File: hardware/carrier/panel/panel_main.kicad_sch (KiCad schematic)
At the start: 27 parts, among them J1 GDEY029T94 FPC, J2 CARRIER, J3 FL-A FPC (FL03), J4 FL-B FPC (Orient), J5 FRONTLIGHT, Q5 SI1308EDL

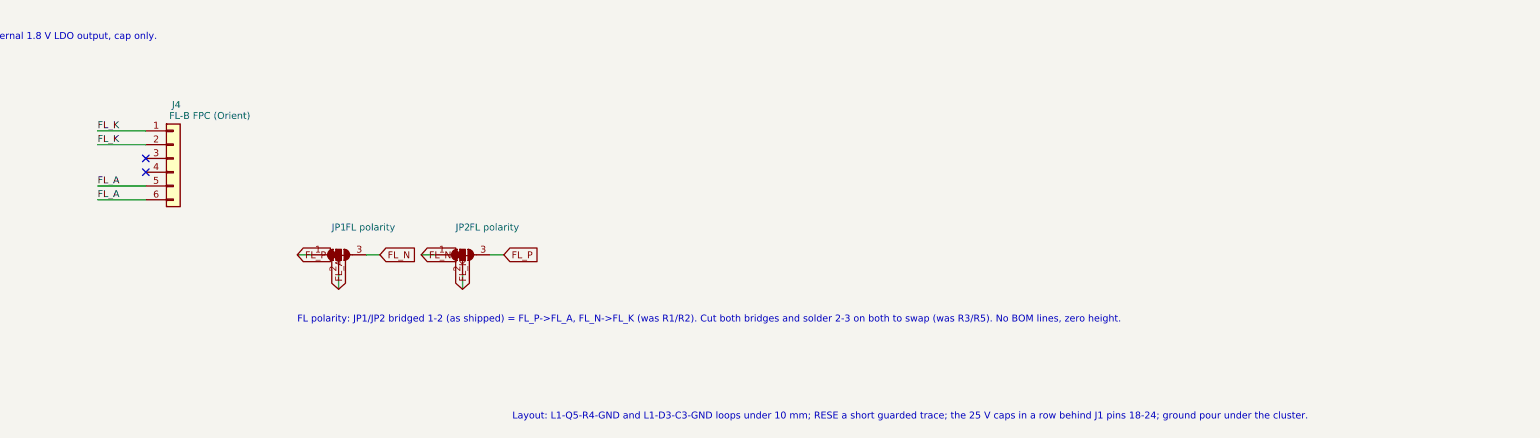
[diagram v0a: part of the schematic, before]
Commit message: Completed the panel board
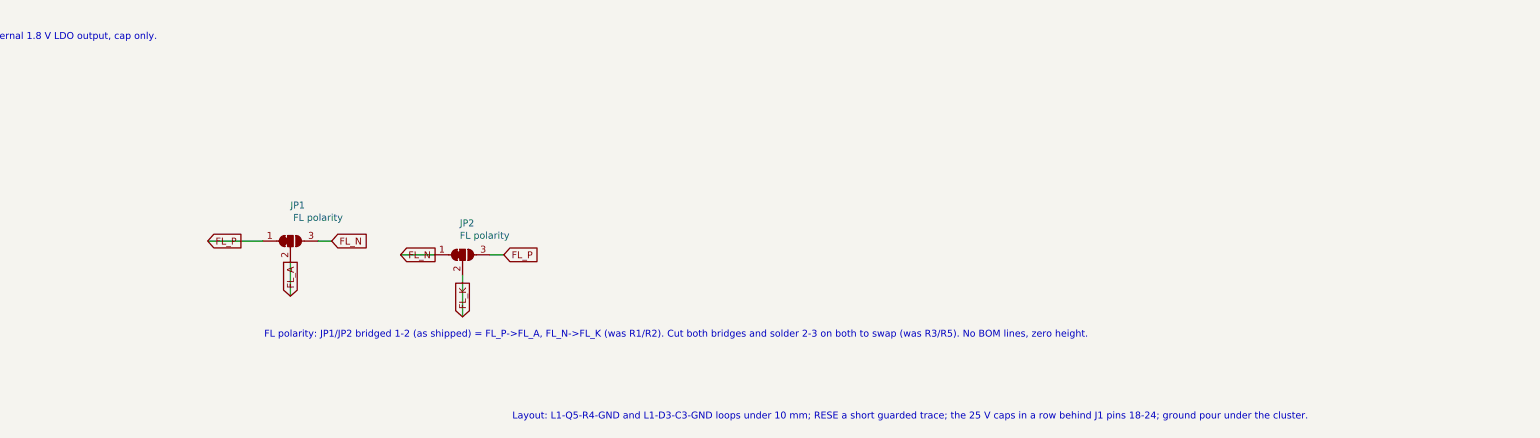
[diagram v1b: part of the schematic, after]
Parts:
- removed J4: FL-B FPC (Orient), pager-carrier:Hirose_FH34SRJ-6S-0.5SH_1x06-1MP_P0.50mm_Horizontal, symbol Connector_Generic:Conn_01x06
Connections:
- no-connect marks 9 -> 7
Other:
- moved on the sheet: JP1
